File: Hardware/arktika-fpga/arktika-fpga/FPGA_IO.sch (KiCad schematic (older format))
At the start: 8 parts

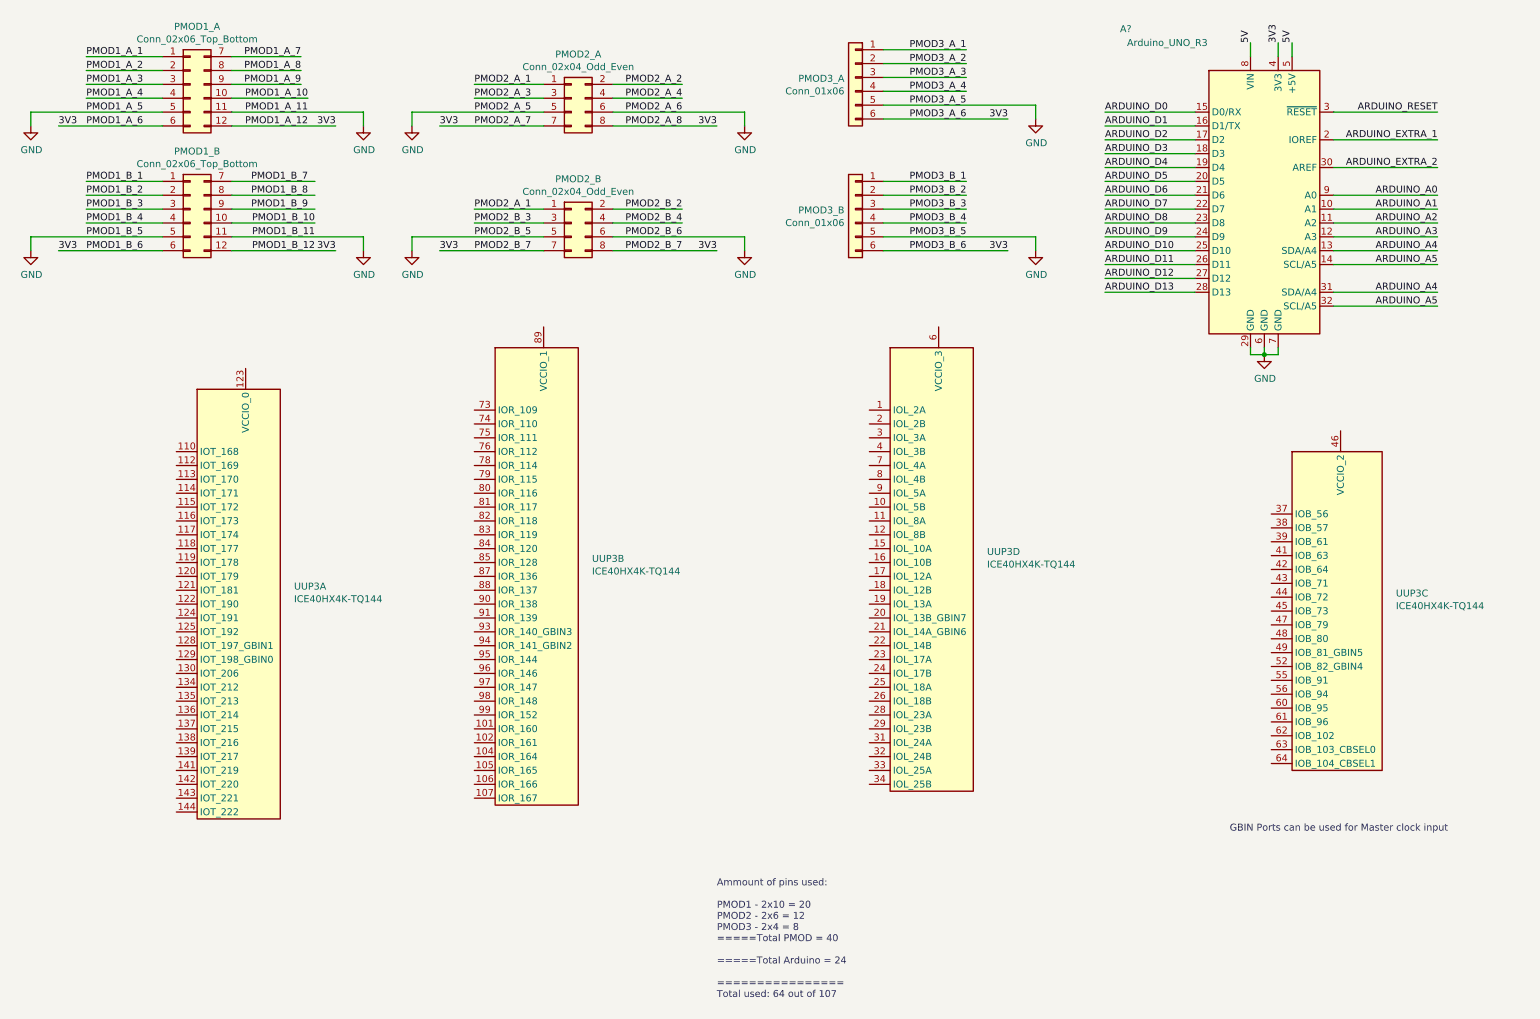
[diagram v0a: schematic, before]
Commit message: Minor fixes, added peripheral buses, added annotations and added crystal datasheets
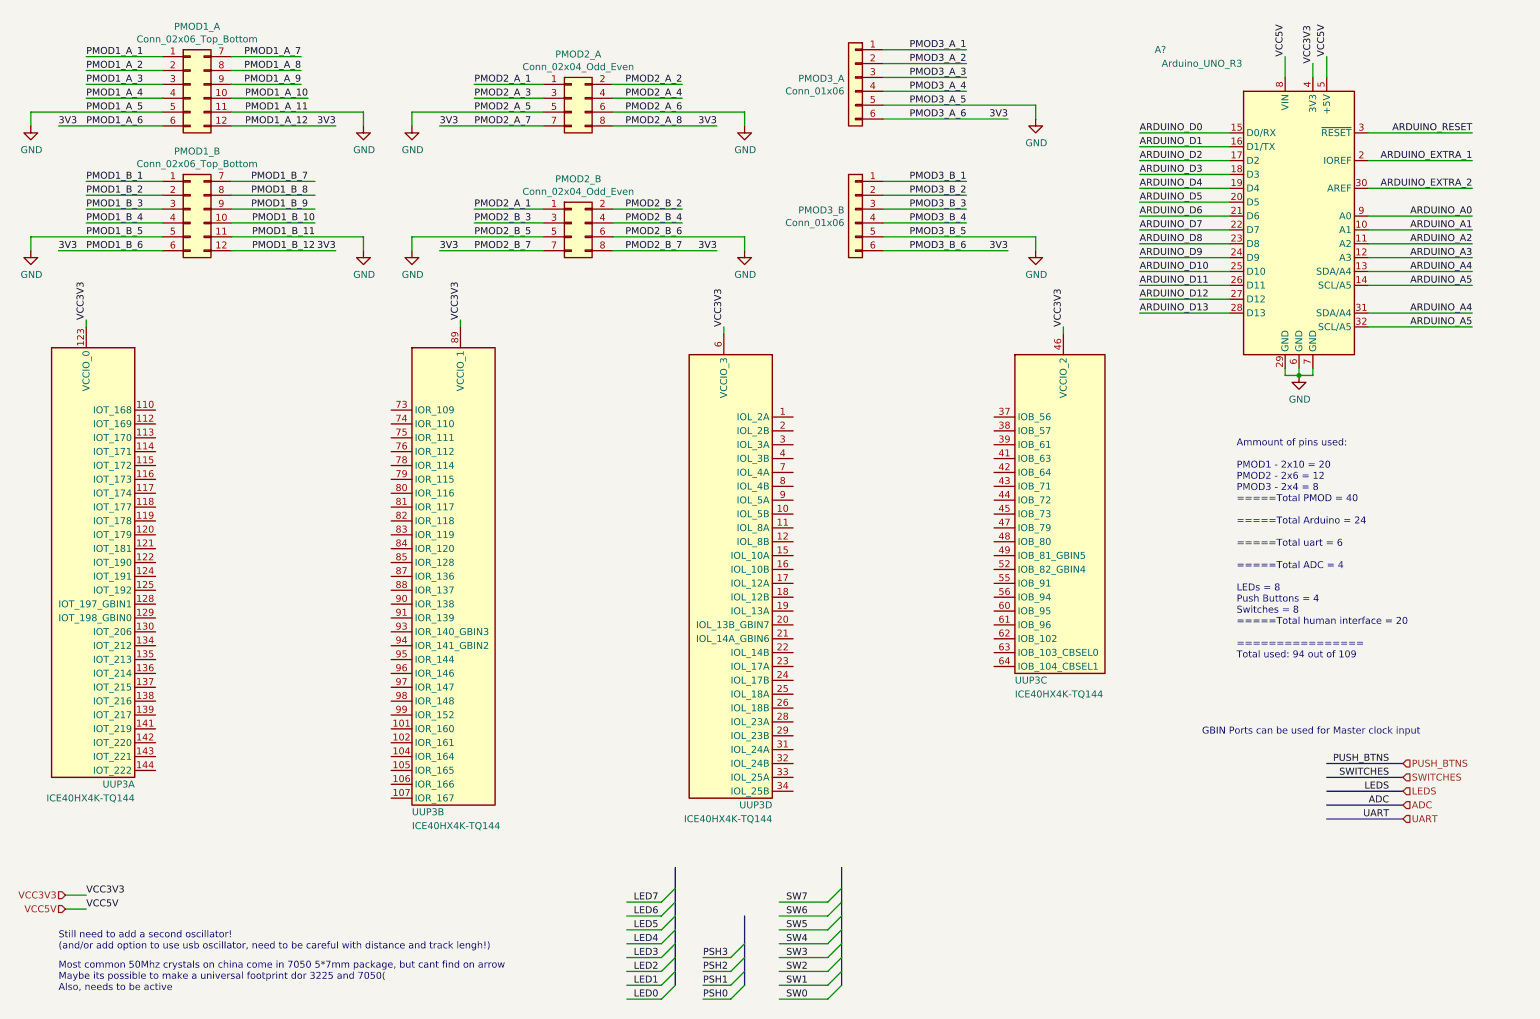
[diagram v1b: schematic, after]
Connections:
- net labels added: ADC, LED0, LED1, LED2, LED3, LED4, LED5, LED6, LED7, LEDS, PSH0, PSH1, PSH2, PSH3, PUSH_BTNS, SW0, SW1, SW2, SW3, SW4, SW5, SW6, SW7, SWITCHES, UART, VCC3V3, VCC5V
- net labels removed: 5V
- wire segments 95 -> 121
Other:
- note added: "Ammount of pins used:\n\nPMOD1 - 2x10 = 20\nPMOD2 - 2x6 = 12\nPMOD3 - 2x4 = 8\n=====Total PMOD = 40\n\n=====Total Arduino = 24\n\n=====Total uart = 6\n\n=====Total ADC = 4\n\nLEDs = 8\nPush Buttons = 4\nSwitches = 8\n=====Total human interface = 20\n\n================\nTotal used: 94 out of 109"
- note added: "Most common 50Mhz crystals on china come in 7050 5*7mm package, but cant find on arrow\nMaybe its possible to make a universal footprint dor 3225 and 7050(\nAlso, needs to be active"
- note added: "Still need to add a second oscillator!\n(and/or add option to use usb oscillator, need to be careful with distance and track lengh!)"
- note removed: "Ammount of pins used:\n\nPMOD1 - 2x10 = 20\nPMOD2 - 2x6 = 12\nPMOD3 - 2x4 = 8\n=====Total PMOD = 40\n\n=====Total Arduino = 24\n\n================\nTotal used: 64 out of 107"
- moved on the sheet: A?, UUP3A, UUP3B, UUP3C, UUP3D

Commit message: Added alternate power intput. Update some designators. Added fpga crystal
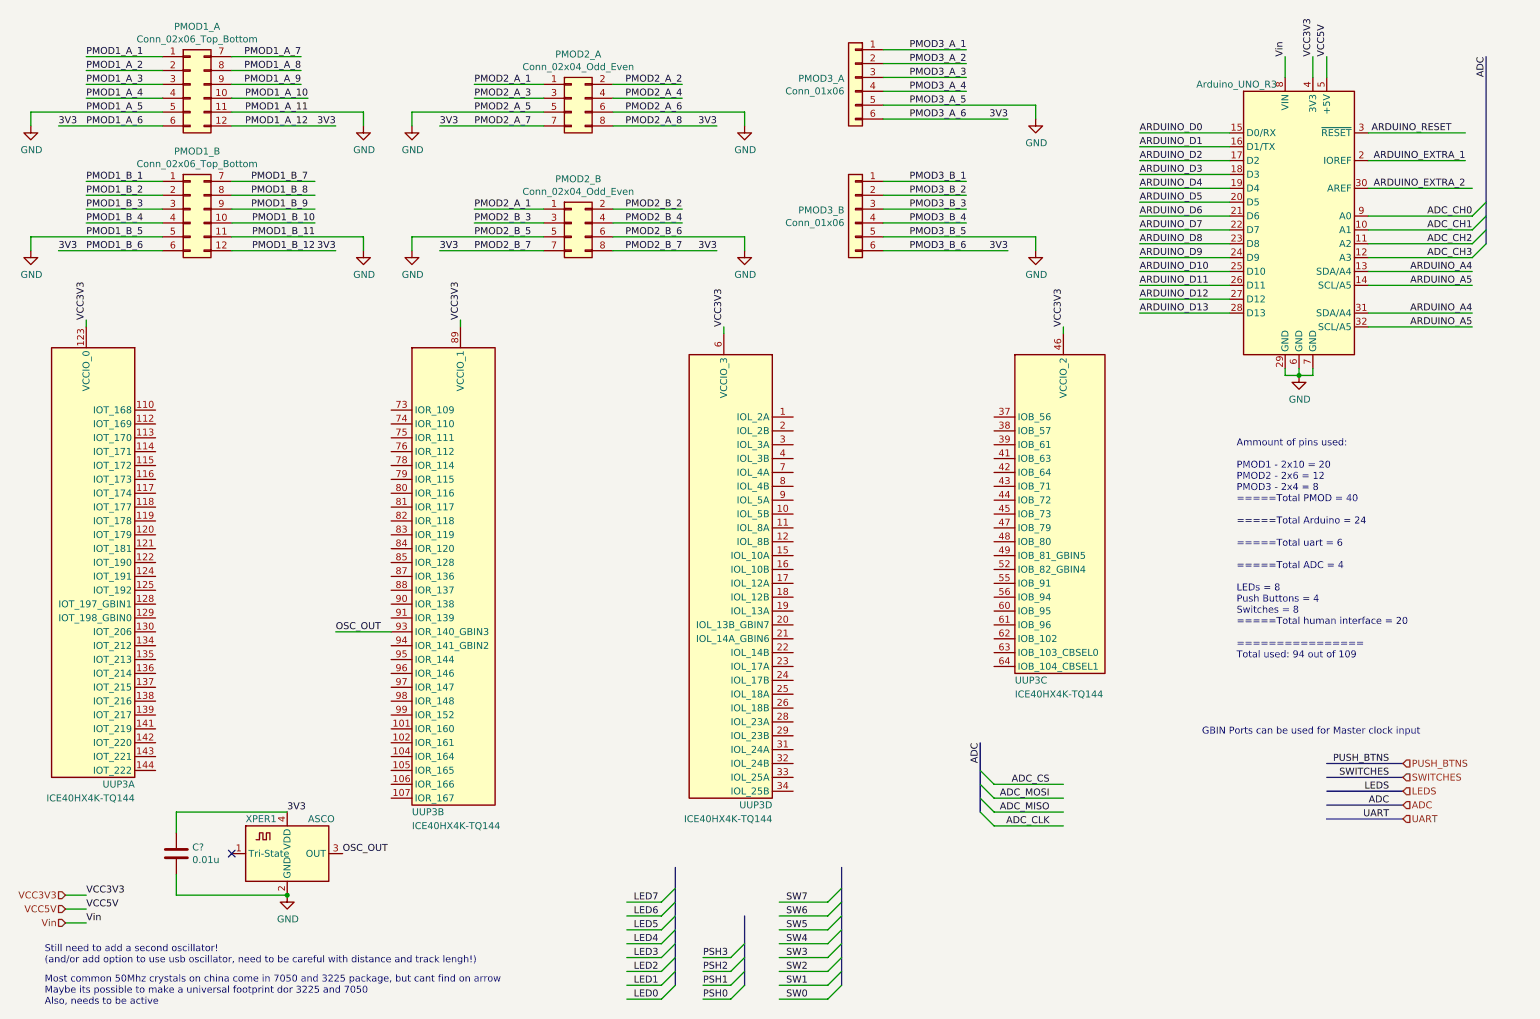
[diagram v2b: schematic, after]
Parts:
- added C?: 0.01u, symbol Device:C
- added XPER1: ASCO, Crystals:Crystal_SMD_3225-4pin_3.2x2.5mm_HandSoldering, symbol Oscillator:ASCO
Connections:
- net labels added: ADC_CH0, ADC_CH1, ADC_CH2, ADC_CH3, ADC_CLK, ADC_CS, ADC_MISO, ADC_MOSI, OSC_OUT, Vin
- net labels removed: ARDUINO_A0, ARDUINO_A1, ARDUINO_A2, ARDUINO_A3
- wire segments 121 -> 131
- no-connect marks 0 -> 1
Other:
- note added: "Most common 50Mhz crystals on china come in 7050 and 3225 package, but cant find on arrow\nMaybe its possible to make a universal footprint dor 3225 and 7050\nAlso, needs to be active"
- note removed: "Most common 50Mhz crystals on china come in 7050 5*7mm package, but cant find on arrow\nMaybe its possible to make a universal footprint dor 3225 and 7050(\nAlso, needs to be active"
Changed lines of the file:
@@
 U 1 1 5F6046D5
 P 9800 1950
-F 0 "A?" H 8800 3150 50  0000 C CNN
-F 1 "Arduino_UNO_R3" H 9100 3050 50  0000 C CNN
+F 0 "A?" H 8800 3150 50  0001 C CNN
+F 1 "Arduino_UNO_R3" H 9350 2900 50  0000 C CNN
 F 2 "Module:Arduino_UNO_R3" H 9800 1950 50  0001 C CIN
 F 3 "https://www.arduino.cc/en/Main/arduinoBoardUno" H 9800 1950 50  0001 C CNN
@@
 Text Label 8650 2650 0    50   ~ 0
 ARDUINO_D13
-Text Label 11050 1950 2    50   ~ 0
-ARDUINO_A0
-Text Label 11050 2050 2    50   ~ 0
-ARDUINO_A1
-Text Label 11050 2150 2    50   ~ 0
-ARDUINO_A2
-Text Label 11050 2250 2    50   ~ 0
-ARDUINO_A3
 Text Label 11050 2350 2    50   ~ 0
 ARDUINO_A4
@@
 Text Label 11050 2750 2    50   ~ 0
 ARDUINO_A5
-Text Label 11050 1550 2    50   ~ 0
+Text Label 11000 1550 2    50   ~ 0
 ARDUINO_EXTRA_1
-Text Label 11050 1750 2    50   ~ 0
+Text Label 11000 1750 2    50   ~ 0
 ARDUINO_EXTRA_2
 Wire Wire Line
@@
 	9300 2650 8650 2650
 Wire Wire Line
-	11050 1550 10300 1550
-Wire Wire Line
 	10300 1750 11050 1750
 Wire Wire Line
-	11050 1950 10300 1950
-Wire Wire Line
-	10300 2050 11050 2050
-Wire Wire Line
-	11050 2150 10300 2150
-Wire Wire Line
-	10300 2250 11050 2250
-Wire Wire Line
 	11050 2350 10300 2350
 Wire Wire Line
@@
 Wire Wire Line
 	10300 2750 11050 2750
-Text Label 11050 1350 2    50   ~ 0
+Text Label 10900 1350 2    50   ~ 0
 ARDUINO_RESET
-Wire Wire Line
-	11050 1350 10300 1350
 Text Notes 9350 5150 0    50   ~ 0
 Ammount of pins used:\n\nPMOD1 - 2x10 = 20\nPMOD2 - 2x6 = 12\nPMOD3 - 2x4 = 8\n=====Total PMOD = 40\n\n=====Total Arduino = 24\n\n=====Total uart = 6\n\n=====Total ADC = 4\n\nLEDs = 8\nPush Buttons = 4\nSwitches = 8\n=====Total human interface = 20\n\n================\nTotal used: 94 out of 109
@@
 Wire Wire Line
 	4850 2200 5600 2200
-Wire Wire Line
-	9900 850  9900 950
 $Comp
 L power:GND #PWR?
@@
 Wire Wire Line
 	1050 2700 1050 2750
-Text Label 9900 850  1    50   ~ 0
+Text Label 9900 800  1    50   ~ 0
 VCC3V3
 Text HLabel 900  6950 0    50   Input ~ 0
@@
 Text Label 10000 800  1    50   ~ 0
 VCC5V
-Text Label 9700 800  1    50   ~ 0
-VCC5V
-Wire Wire Line
-	9700 800  9700 950
 Wire Wire Line
 	10000 800  10000 950
@@
 Text Label 10450 6300 2    50   ~ 0
 UART
-Text Notes 850  7250 0    50   ~ 0
+Text Notes 750  7350 0    50   ~ 0
 Still need to add a second oscillator!\n(and/or add option to use usb oscillator, need to be careful with distance and track lengh!)
-Text Notes 850  7550 0    50   ~ 0
-Most common 50Mhz crystals on china come in 7050 5*7mm package, but cant find on arrow\nMaybe its possible to make a universal footprint dor 3225 and 7050(\nAlso, needs to be active
+Text Notes 750  7650 0    50   ~ 0
+Most common 50Mhz crystals on china come in 7050 and 3225 package, but cant find on arrow\nMaybe its possible to make a universal footprint dor 3225 and 7050\nAlso, needs to be active
+$Comp
+L Oscillator:ASCO XPER1
+U 1 1 5F23DFDD
+P 2500 6550
+F 0 "XPER1" H 2200 6800 50  0000 L CNN
+F 1 "ASCO" H 2650 6800 50  0000 L CNN
+F 2 "Crystals:Crystal_SMD_3225-4pin_3.2x2.5mm_HandSoldering" H 2600 6200 50  0001 C CNN
+F 3 "https://abracon.com/Oscillators/ASCO.pdf" H 2275 6675 50  0001 C CNN
+	1    2500 6550
+	1    0    0    -1
+$EndComp
+$Comp
+L Device:C C?
+U 1 1 5F23EF40
+P 1700 6550
+F 0 "C?" H 1815 6596 50  0000 L CNN
+F 1 "0.01u" H 1815 6505 50  0000 L CNN
+F 2 "" H 1738 6400 50  0001 C CNN
+F 3 "~" H 1700 6550 50  0001 C CNN
+	1    1700 6550
+	1    0    0    -1
+$EndComp
+Wire Wire Line
+	1700 6400 1700 6250
+Wire Wire Line
+	1700 6250 2500 6250
+Wire Wire Line
+	2500 6850 1700 6850
+Wire Wire Line
+	1700 6850 1700 6700
+$Comp
+L power:GND #PWR?
+U 1 1 5F24D370
+P 2500 6850
+F 0 "#PWR?" H 2500 6600 50  0001 C CNN
+F 1 "GND" H 2505 6677 50  0000 C CNN
+F 2 "" H 2500 6850 50  0001 C CNN
+F 3 "" H 2500 6850 50  0001 C CNN
+	1    2500 6850
+	1    0    0    -1
+$EndComp
+Connection ~ 2500 6850
+Text Label 2500 6250 0    50   ~ 0
+3V3
+Text Label 2900 6550 0    50   ~ 0
+OSC_OUT
+Text Label 2850 4950 0    50   ~ 0
+OSC_OUT
+Wire Wire Line
+	2850 4950 3250 4950
+NoConn ~ 2100 6550
+Entry Wire Line
+	11050 2250 11150 2150
+Entry Wire Line
+	11050 2150 11150 2050
+Entry Wire Line
+	11050 2050 11150 1950
+Entry Wire Line
+	11050 1950 11150 1850
+Text Label 11050 1950 2    50   ~ 0
+ADC_CH0
+Text Label 11050 2050 2    50   ~ 0
+ADC_CH1
+Text Label 11050 2150 2    50   ~ 0
+ADC_CH2
+Text Label 11050 2250 2    50   ~ 0
+ADC_CH3
+Text Label 11150 800  3    50   ~ 0
+ADC
+Entry Wire Line
+	7600 6350 7500 6250
+Entry Wire Line
+	7600 6250 7500 6150
+Entry Wire Line
+	7600 6150 7500 6050
+Entry Wire Line
+	7600 6050 7500 5950
+Text Label 8000 6350 2    50   ~ 0
+ADC_CLK
+Text Label 8000 6250 2    50   ~ 0
+ADC_MISO
+Text Label 8000 6150 2    50   ~ 0
+ADC_MOSI
+Text Label 8000 6050 2    50   ~ 0
+ADC_CS
+Wire Wire Line
+	8100 6350 7600 6350
+Wire Wire Line
+	7600 6250 8100 6250
+Wire Wire Line
+	8100 6150 7600 6150
+Wire Wire Line
+	7600 6050 8100 6050
+Text Label 7500 5750 3    50   ~ 0
+ADC
+Wire Wire Line
+	10300 1950 11050 1950
+Wire Wire Line
+	10300 2050 11050 2050
+Wire Wire Line
+	10300 2150 11050 2150
+Wire Wire Line
+	10300 2250 11050 2250
+Wire Wire Line
+	10300 1550 11000 1550
+Wire Wire Line
+	11000 1350 10300 1350
+Text Label 9700 800  1    50   ~ 0
+Vin
+Wire Wire Line
+	9700 800  9700 950
+Wire Wire Line
+	9900 800  9900 950
+Text HLabel 900  7050 0    50   Input ~ 0
+Vin
+Wire Wire Line
+	900  7050 1050 7050
+Text Label 1050 7050 0    50   ~ 0
+Vin
 Wire Bus Line
 	5800 7000 5800 7500
 Wire Bus Line
+	7500 5750 7500 6250
+Wire Bus Line
+	11150 800  11150 2150
+Wire Bus Line
 	6500 6650 6500 7500

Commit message: Misc changes and fixes
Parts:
- gave numbers to parts that had none: 1
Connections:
- net labels added: Buzzer
- wire segments 131 -> 133
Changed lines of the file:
@@
 	6800 2000 7400 2000
 $Comp
-L MCU_Module:Arduino_UNO_R3 A?
+L MCU_Module:Arduino_UNO_R3 A1
 U 1 1 5F6046D5
 P 9800 1950
-F 0 "A?" H 8800 3150 50  0001 C CNN
+F 0 "A1" H 8800 3150 50  0001 C CNN
 F 1 "Arduino_UNO_R3" H 9350 2900 50  0000 C CNN
 F 2 "Module:Arduino_UNO_R3" H 9800 1950 50  0001 C CIN
@@
 3V3
 $Comp
-L power:GND #PWR?
+L power:GND #PWR0134
 U 1 1 5F669A5F
 P 3400 1300
-F 0 "#PWR?" H 3400 1050 50  0001 C CNN
+F 0 "#PWR0134" H 3400 1050 50  0001 C CNN
 F 1 "GND" H 3405 1127 50  0000 C CNN
 F 2 "" H 3400 1300 50  0001 C CNN
@@
 $EndComp
 $Comp
-L power:GND #PWR?
+L power:GND #PWR0135
 U 1 1 5F66A4F2
 P 5800 1300
-F 0 "#PWR?" H 5800 1050 50  0001 C CNN
+F 0 "#PWR0135" H 5800 1050 50  0001 C CNN
 F 1 "GND" H 5805 1127 50  0000 C CNN
 F 2 "" H 5800 1300 50  0001 C CNN
@@
 3V3
 $Comp
-L power:GND #PWR?
+L power:GND #PWR0136
 U 1 1 5F67B3BB
 P 3400 2200
-F 0 "#PWR?" H 3400 1950 50  0001 C CNN
+F 0 "#PWR0136" H 3400 1950 50  0001 C CNN
 F 1 "GND" H 3405 2027 50  0000 C CNN
 F 2 "" H 3400 2200 50  0001 C CNN
@@
 3V3
 $Comp
-L power:GND #PWR?
+L power:GND #PWR0137
 U 1 1 5F6821AA
 P 5800 2200
-F 0 "#PWR?" H 5800 1950 50  0001 C CNN
+F 0 "#PWR0137" H 5800 1950 50  0001 C CNN
 F 1 "GND" H 5805 2027 50  0000 C CNN
 F 2 "" H 5800 2200 50  0001 C CNN
@@
 	4850 2200 5600 2200
 $Comp
-L power:GND #PWR?
+L power:GND #PWR0138
 U 1 1 5F6931F6
 P 9800 3100
-F 0 "#PWR?" H 9800 2850 50  0001 C CNN
+F 0 "#PWR0138" H 9800 2850 50  0001 C CNN
 F 1 "GND" H 9805 2927 50  0000 C CNN
 F 2 "" H 9800 3100 50  0001 C CNN
@@
 3V3
 $Comp
-L power:GND #PWR?
+L power:GND #PWR0139
 U 1 1 5F694E96
 P 7900 1250
-F 0 "#PWR?" H 7900 1000 50  0001 C CNN
+F 0 "#PWR0139" H 7900 1000 50  0001 C CNN
 F 1 "GND" H 7905 1077 50  0000 C CNN
 F 2 "" H 7900 1250 50  0001 C CNN
@@
 3V3
 $Comp
-L power:GND #PWR?
+L power:GND #PWR0140
 U 1 1 5F698C2B
 P 7900 2200
-F 0 "#PWR?" H 7900 1950 50  0001 C CNN
+F 0 "#PWR0140" H 7900 1950 50  0001 C CNN
 F 1 "GND" H 7905 2027 50  0000 C CNN
 F 2 "" H 7900 2200 50  0001 C CNN
@@
 3V3
 $Comp
-L power:GND #PWR?
+L power:GND #PWR0141
 U 1 1 5F6B0B31
 P 650 1300
-F 0 "#PWR?" H 650 1050 50  0001 C CNN
+F 0 "#PWR0141" H 650 1050 50  0001 C CNN
 F 1 "GND" H 655 1127 50  0000 C CNN
 F 2 "" H 650 1300 50  0001 C CNN
@@
 3V3
 $Comp
-L power:GND #PWR?
+L power:GND #PWR0142
 U 1 1 5F6B4646
 P 650 2200
-F 0 "#PWR?" H 650 1950 50  0001 C CNN
+F 0 "#PWR0142" H 650 1950 50  0001 C CNN
 F 1 "GND" H 655 2027 50  0000 C CNN
 F 2 "" H 650 2200 50  0001 C CNN
@@
 3V3
 $Comp
-L power:GND #PWR?
+L power:GND #PWR0143
 U 1 1 5F6B815F
 P 3050 1300
-F 0 "#PWR?" H 3050 1050 50  0001 C CNN
+F 0 "#PWR0143" H 3050 1050 50  0001 C CNN
 F 1 "GND" H 3055 1127 50  0000 C CNN
 F 2 "" H 3050 1300 50  0001 C CNN
@@
 3V3
 $Comp
-L power:GND #PWR?
+L power:GND #PWR0144
 U 1 1 5F6BBFC9
 P 3050 2200
-F 0 "#PWR?" H 3050 1950 50  0001 C CNN
+F 0 "#PWR0144" H 3050 1950 50  0001 C CNN
 F 1 "GND" H 3055 2027 50  0000 C CNN
 F 2 "" H 3050 2200 50  0001 C CNN
@@
 	1700 6850 1700 6700
 $Comp
-L power:GND #PWR?
+L power:GND #PWR0145
 U 1 1 5F24D370
 P 2500 6850
-F 0 "#PWR?" H 2500 6600 50  0001 C CNN
+F 0 "#PWR0145" H 2500 6600 50  0001 C CNN
 F 1 "GND" H 2505 6677 50  0000 C CNN
 F 2 "" H 2500 6850 50  0001 C CNN
@@
 Text Label 1050 7050 0    50   ~ 0
 Vin
+Text HLabel 10550 6400 2    50   Input ~ 0
+Buzzer
+Wire Wire Line
+	10550 6400 10000 6400
+Text Label 10450 6400 2    50   ~ 0
+Buzzer
+Text HLabel 900  6500 0    50   Input ~ 0
+GND
+$Comp
+L power:GND #PWR?
+U 1 1 5F2CF44B
+P 1200 6500
+AR Path="/5F2CF44B" Ref="#PWR?"  Part="1"
+AR Path="/5F3E98C5/5F2CF44B" Ref="#PWR?"  Part="1"
+AR Path="/5F516611/5F2CF44B" Ref="#PWR0146"  Part="1"
+F 0 "#PWR0146" H 1200 6250 50  0001 C CNN
+F 1 "GND" H 1200 6350 50  0000 C CNN
+F 2 "" H 1200 6500 50  0001 C CNN
+F 3 "" H 1200 6500 50  0001 C CNN
+	1    1200 6500
+	1    0    0    -1
+$EndComp
+Wire Wire Line
+	1200 6500 900  6500
 Wire Bus Line
 	5800 7000 5800 7500
